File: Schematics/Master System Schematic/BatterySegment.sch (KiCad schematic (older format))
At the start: 148 parts

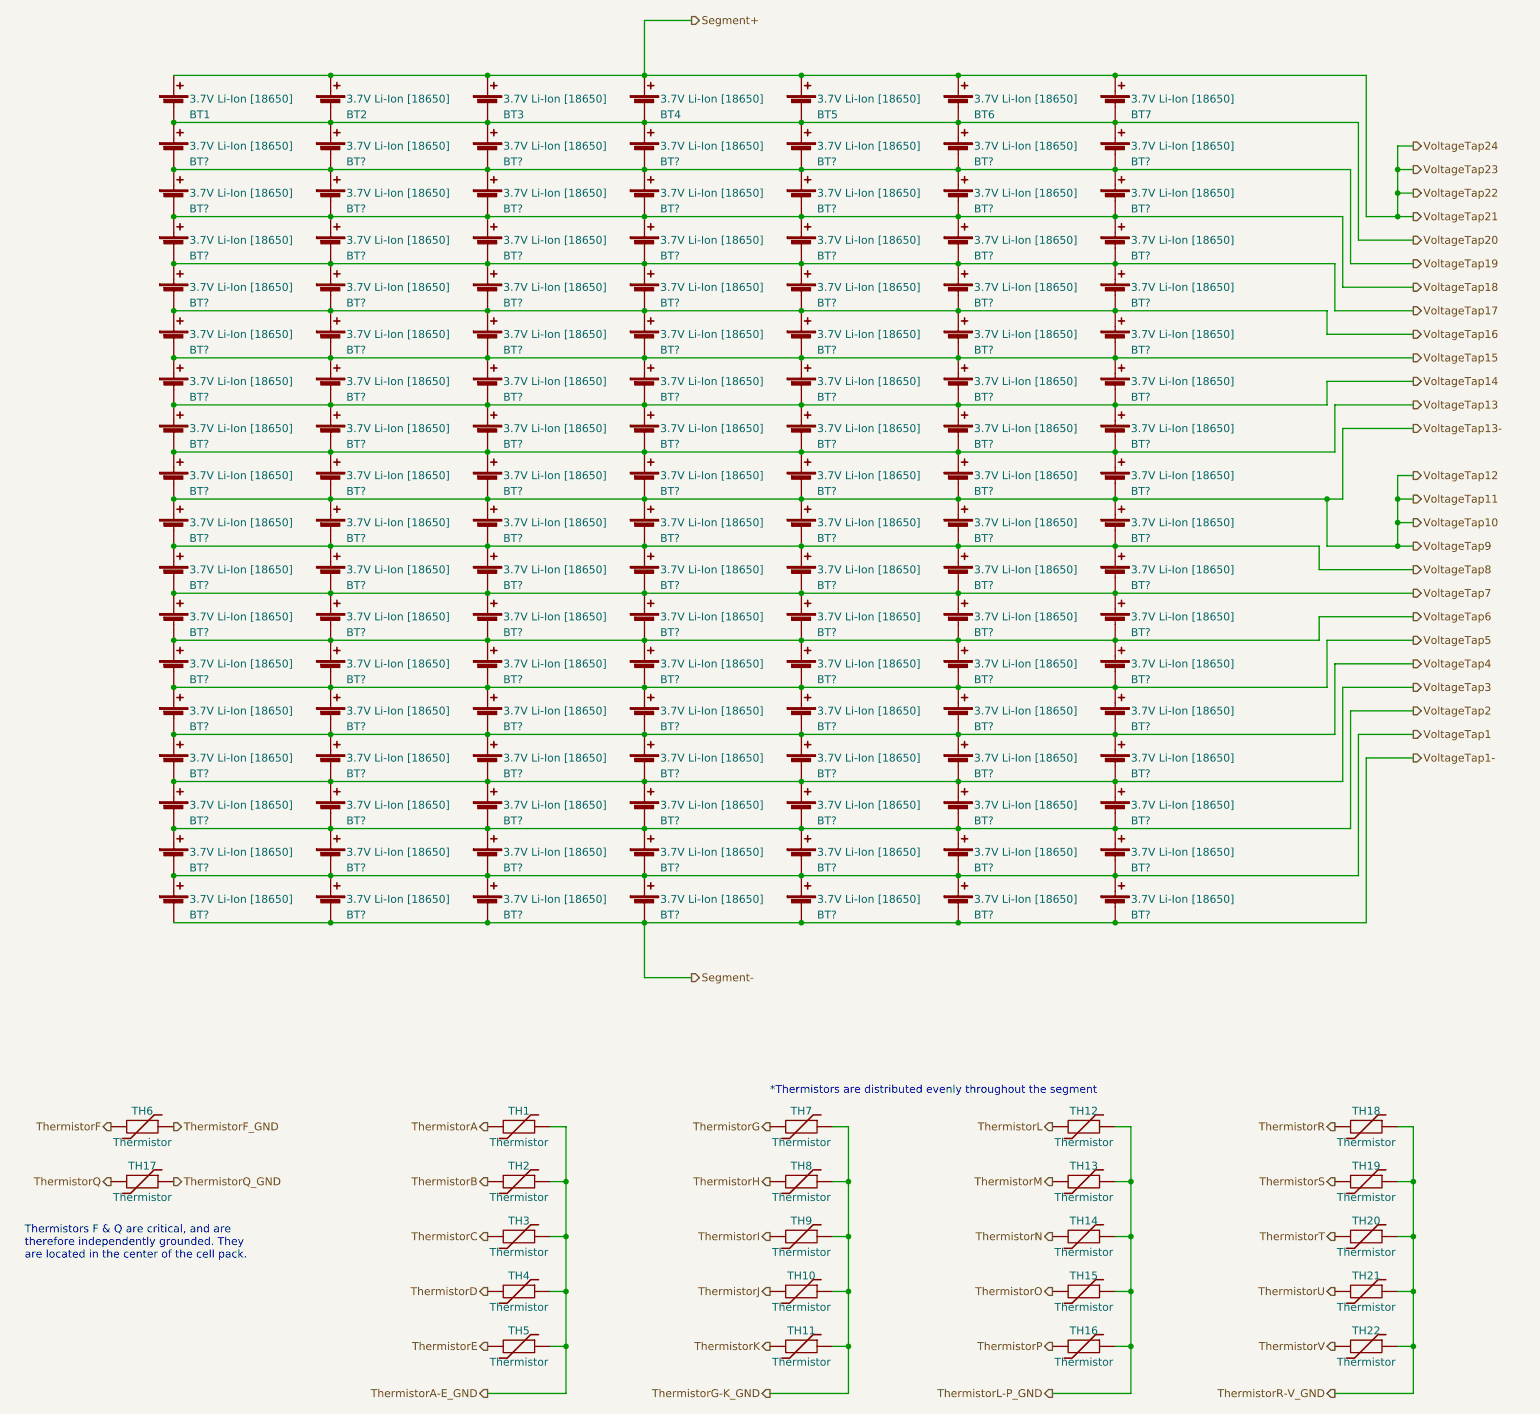
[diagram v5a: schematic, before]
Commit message: Connectors and Start of Numbering
Created new generic connectors and applied numbering tool to whole project
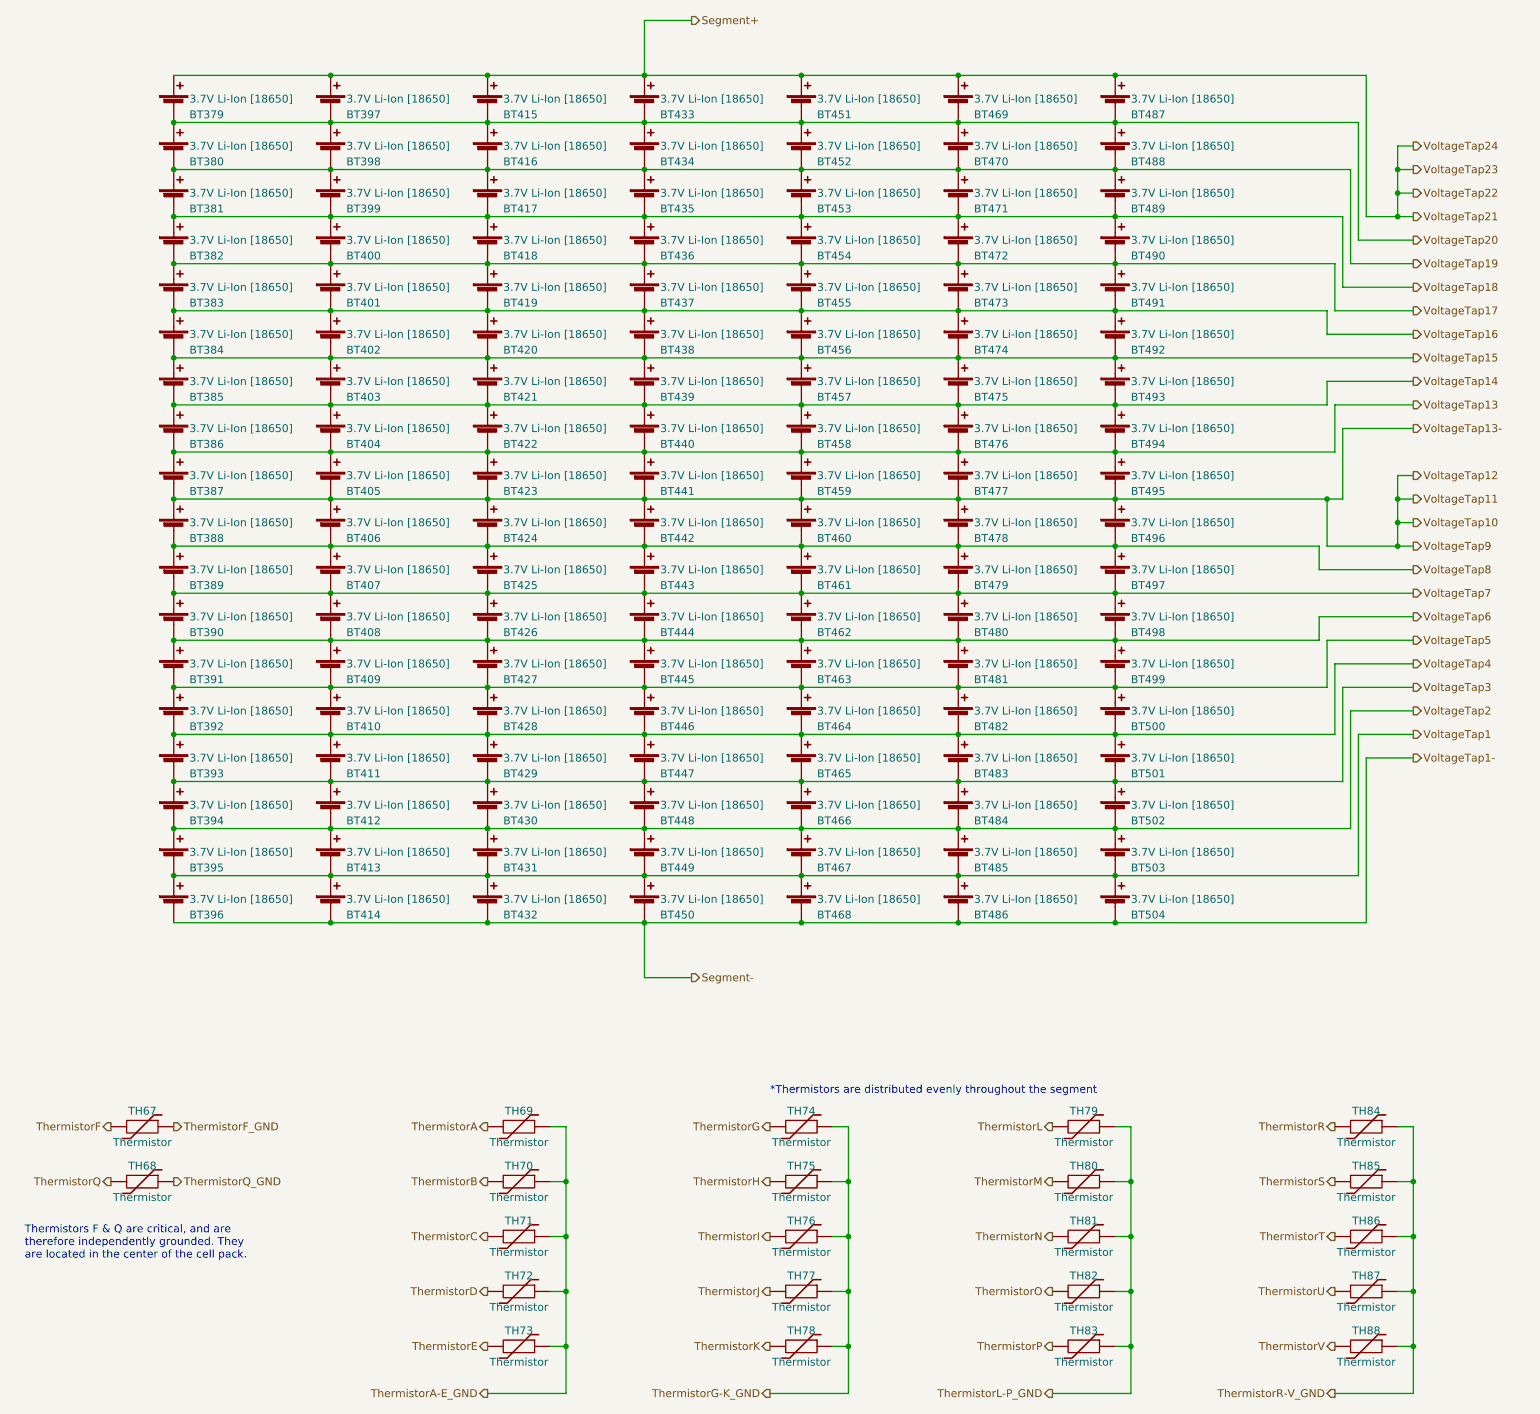
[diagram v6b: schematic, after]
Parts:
- gave numbers to parts that had none: 119
